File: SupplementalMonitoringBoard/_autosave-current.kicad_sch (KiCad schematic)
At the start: 8 parts, among them U2 OPA842xDBV

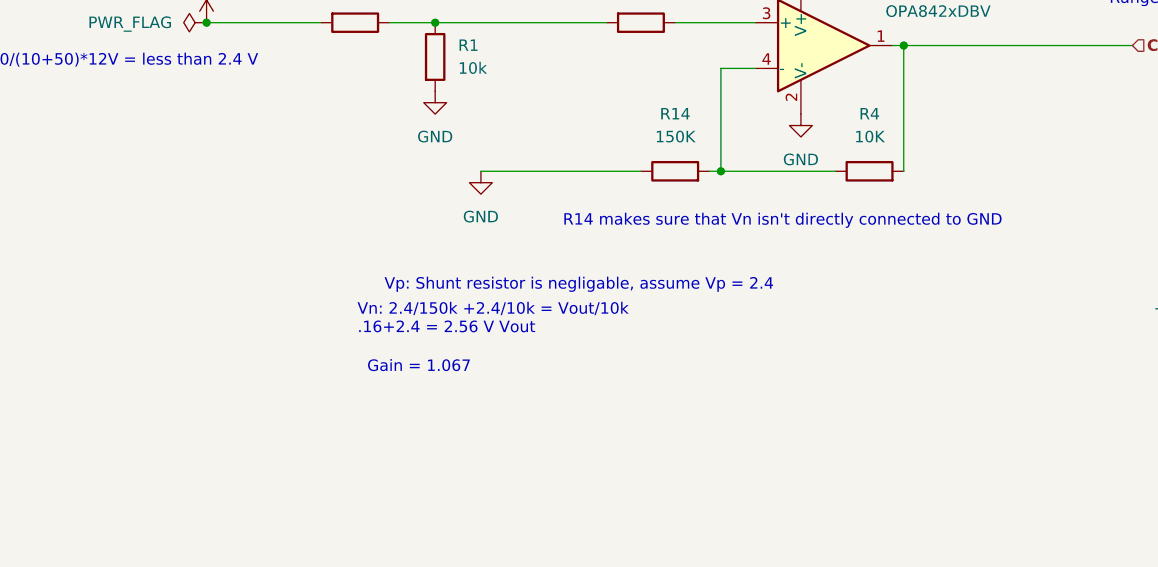
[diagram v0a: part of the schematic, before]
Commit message: PCB Layout - Supplemental Monitoring Board
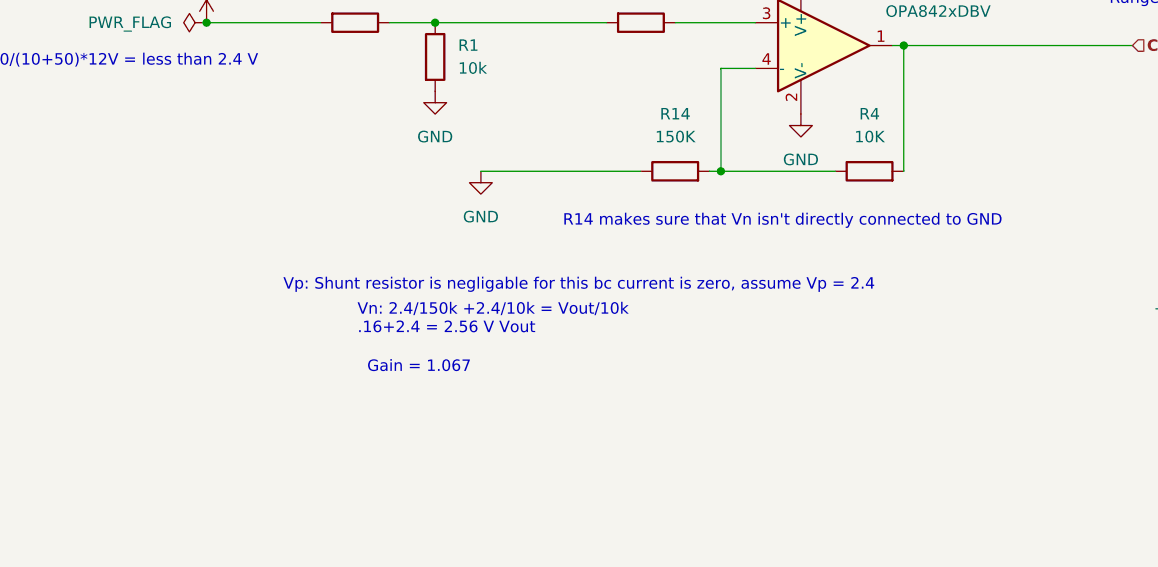
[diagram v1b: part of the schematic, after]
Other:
- note added: "Vp: Shunt resistor is negligable for this bc current is zero, assume Vp = 2.4"
- note removed: "Vp: Shunt resistor is negligable, assume Vp = 2.4"
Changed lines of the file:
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@@
 		)
 	)
-	(text "Vp: Shunt resistor is negligable, assume Vp = 2.4\n"
+	(text "Vp: Shunt resistor is negligable for this bc current is zero, assume Vp = 2.4\n"
 		(exclude_from_sim no)
 		(at 113.792 119.38 0)
